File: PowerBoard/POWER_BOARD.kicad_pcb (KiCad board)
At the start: 4 copper layers, 152.1 x 80.1 mm, 158 parts, among them J1 B3B-XH-A_LF__SN_, J2 USB4145-03-0170-C_REVA2, J3 Molex Microfit 3.0, J5 Conn_02x10_Counter_Clockwise, J6 Molex Microfit 3.0, Q1 BSS138, Q2 FDD86250-F085, Q3 FGH50T65SQD-F155, Q4 BSS138, Q5 TN2130K1-G, Q6 STD11N60DM2, Q7 FGH50T65SQD-F155, T1 DA2034, U1 RPI2040, U10 PTS647SM38SMTR2LFS, U2 MCP14A0454-E/SN, U3 NCV1117DT33T5G, U4 LT3750, U5 W25Q16JVSNIQ, U6 LTC4151IMS_PBF, U7 MCP2515-xST, U8 MCP2551-I-SN, U9 PTS647SM38SMTR2LFS, Y1 ABM3-12.000MHZ-D2Y-T, Y2 ABM3-8.000MHZ-D2Y-T

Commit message: passed DRC check
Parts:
- Y2: footprint bots:445C25D12M00000 -> bots:ABM3
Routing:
- net Net-(C25-Pad2): track 6.77 -> 6.05 mm

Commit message: added pdfs
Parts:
- moved C2 52.2 mm to (119.7, 62.1)
- moved C3 52.2 mm to (119.7, 60.0)
- moved TP22 52.2 mm to (86.8, 64.6)
- moved R1 52.2 mm to (97.0, 58.0)
- moved R14 52.2 mm to (65.5, 42.5)
- moved R15 52.2 mm to (70.5, 42.5)
- moved R25 52.2 mm to (86.3, 45.9)
- moved TP17 52.2 mm to (109.8, 49.5)
- moved TP2 52.2 mm to (136.6, 41.4)
- moved TP9 52.2 mm to (117.4, 42.1)
- moved C13 52.2 mm to (74.3, 54.7)
- moved C15 52.2 mm to (83.0, 45.6)
- moved C19 52.2 mm to (75.0, 60.4)
- moved C20 52.2 mm to (90.1, 53.8)
- moved C23 52.2 mm to (90.1, 52.0)
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
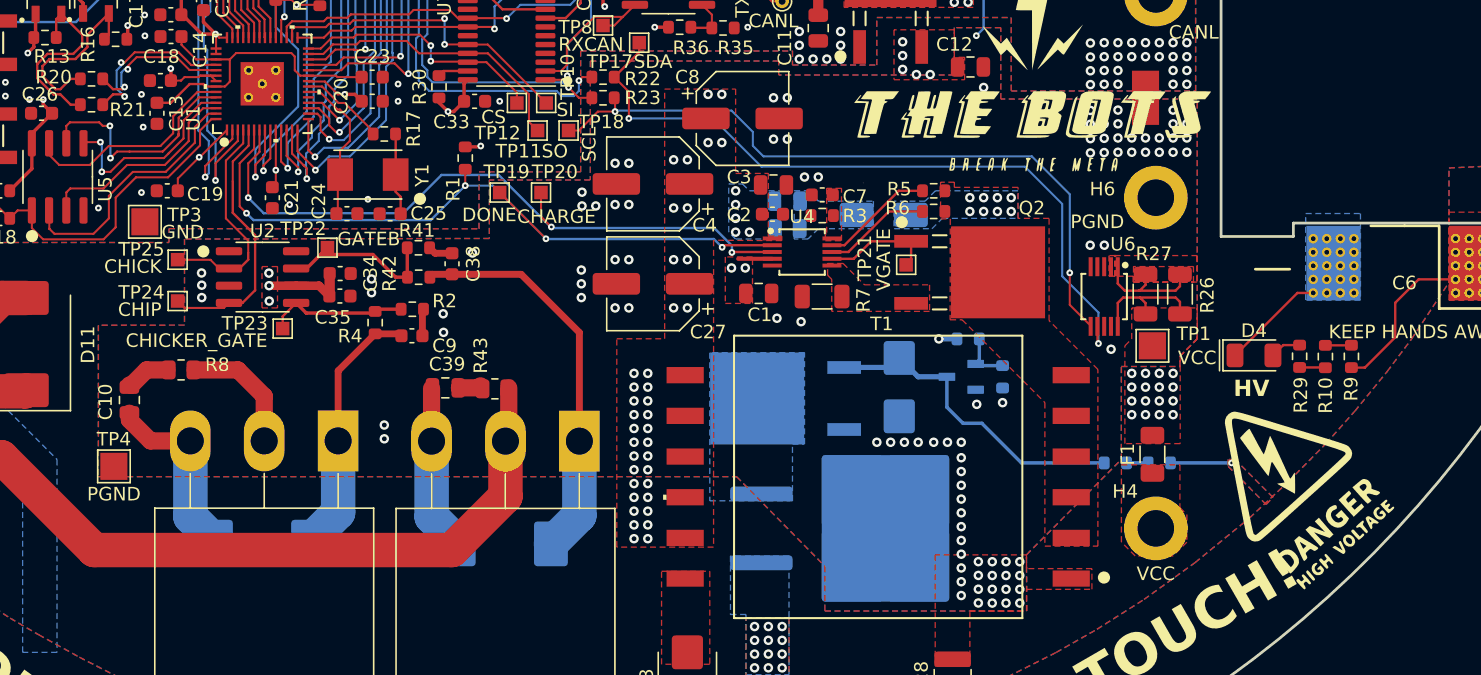
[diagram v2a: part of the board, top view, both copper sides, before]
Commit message: update to power board and midplate schematics
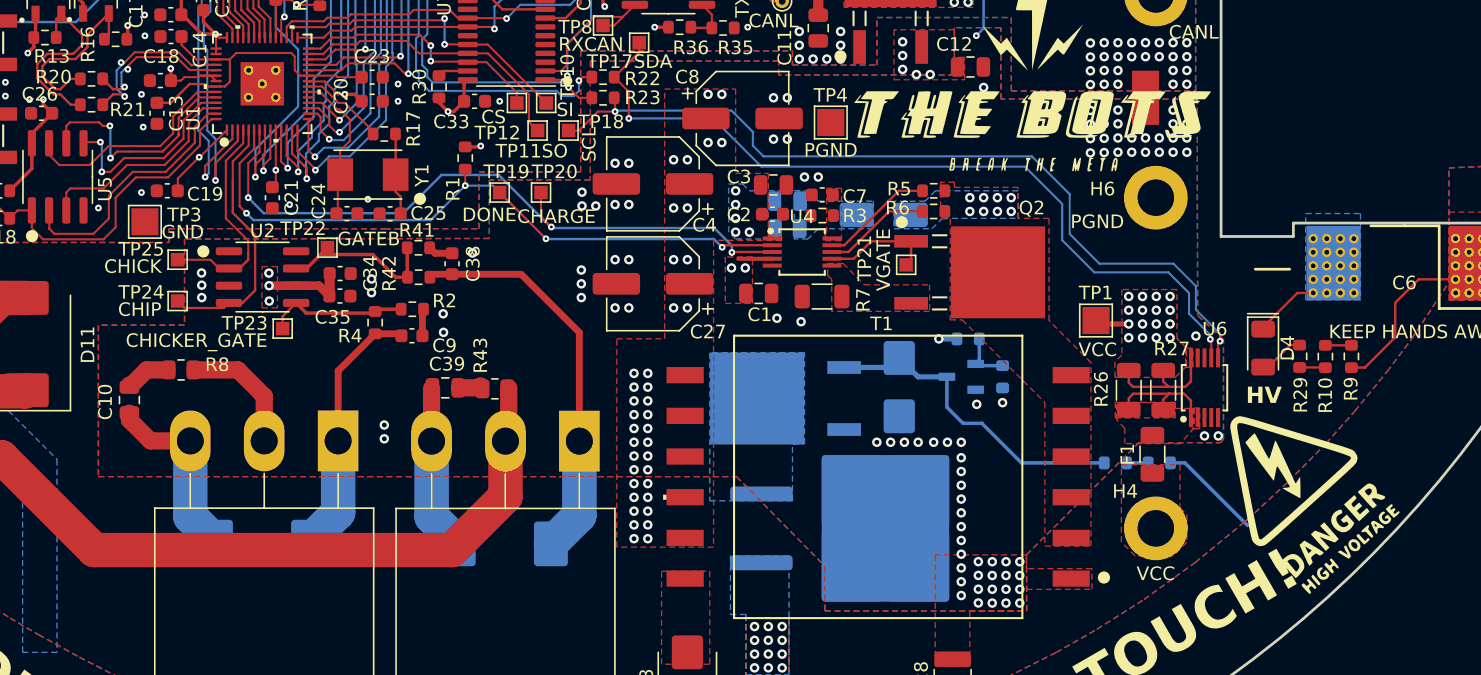
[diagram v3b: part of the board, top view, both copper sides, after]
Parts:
- moved TP4 58.6 mm to (124.0, 55.4)
- moved U6 10.00 mm to (151.5, 74.9), turned to 90 degrees
- moved R26 8.03 mm to (145.9, 75.1), turned to 90 degrees
- moved R27 7.21 mm to (148.5, 75.1), turned to 90 degrees
- moved TP1 4.56 mm to (143.5, 70.0)
- moved D4 0.86 mm to (155.8, 72.0), turned to -90 degrees
- moved G*** 0.52 mm to (158.1, 82.2)
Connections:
- F1 pad 2: VCC -> /Power/VCC_RPP
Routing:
- net /Power/U6SCL: track 52.1 -> 61.7 mm
- net /Power/U6SDA: track 54.1 -> 60.5 mm
- net HV: track 21.4 -> 24.5 mm, vias 13 -> 12
- net GNDPWR: track 37.7 -> 35.0 mm
- net VCC: track 31.1 -> 33.6 mm
- net Net-(D4-A): track 2.28 -> 3.37 mm

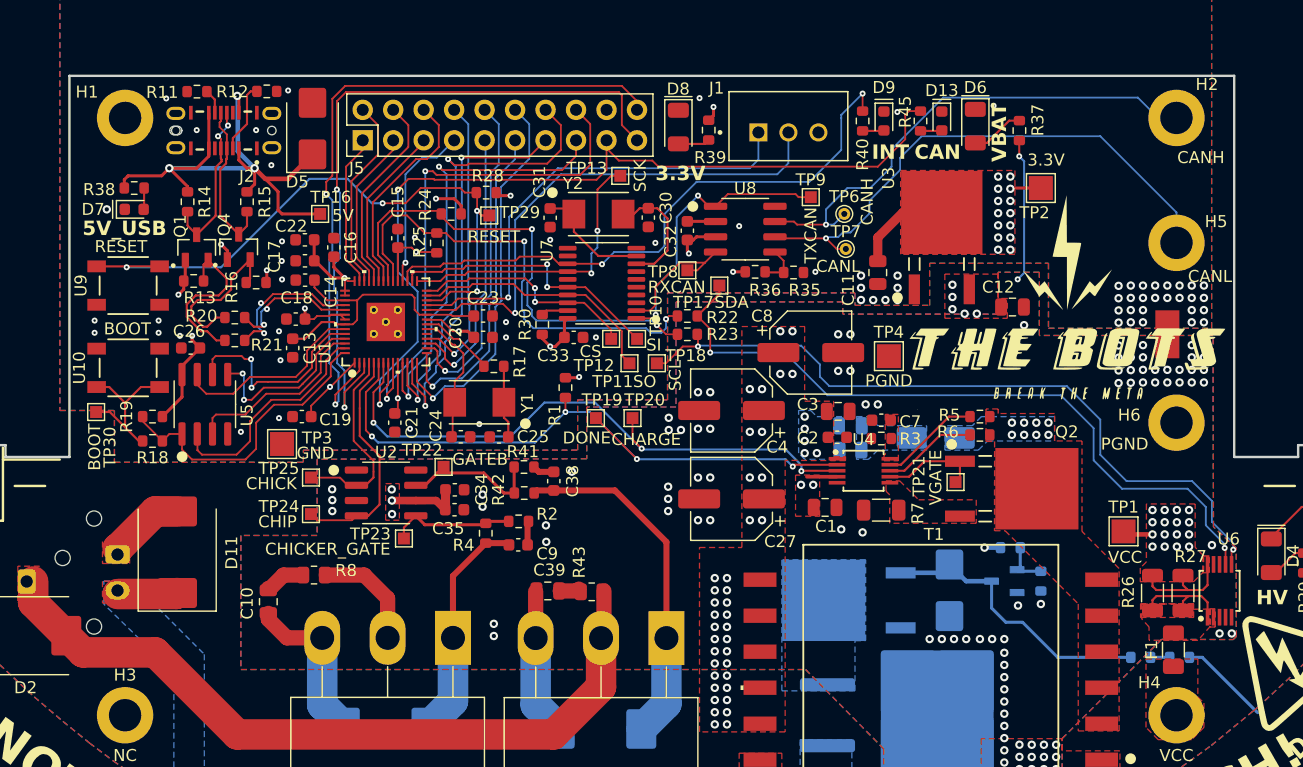
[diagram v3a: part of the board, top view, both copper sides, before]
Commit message: added switch and fuse
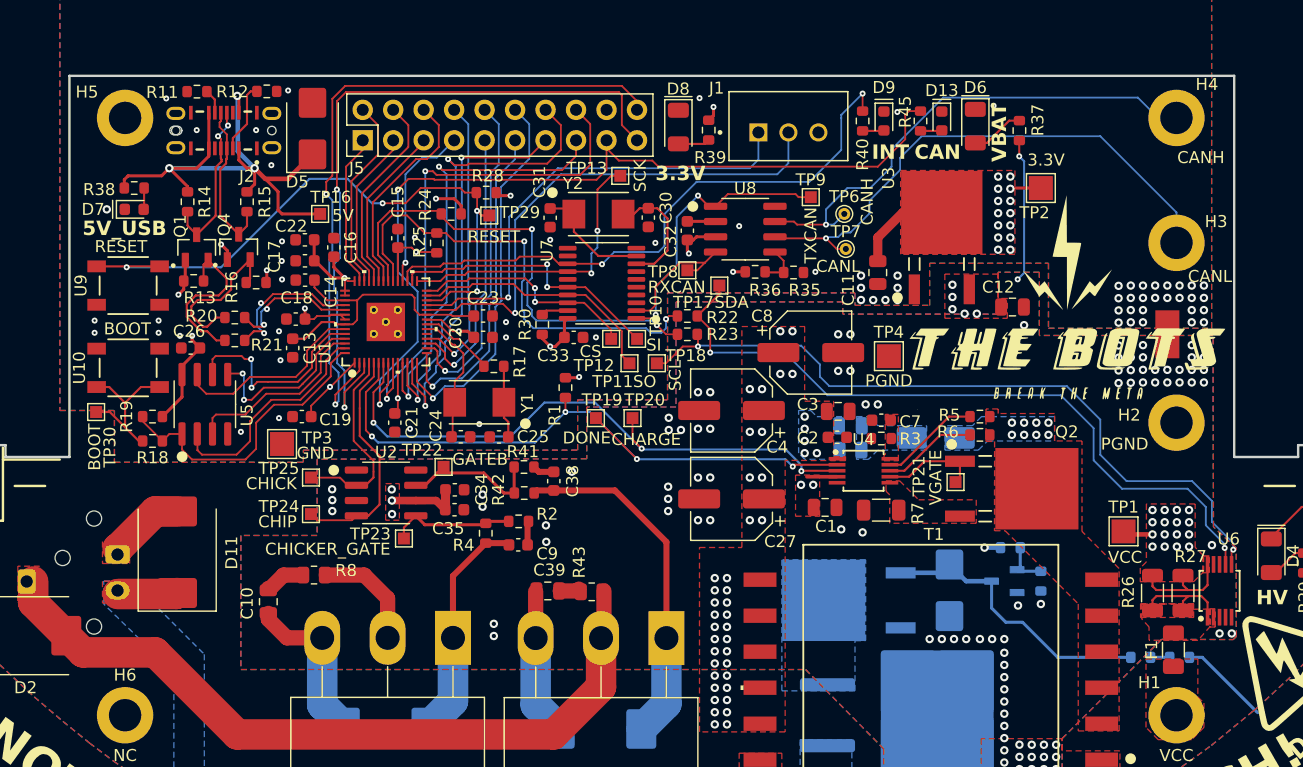
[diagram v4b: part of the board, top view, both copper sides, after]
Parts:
- renumbered H4 to H1, H6 to H2, H5 to H3, H2 to H4, H1 to H5, H3 to H6
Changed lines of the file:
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@@
   (net 108 "/Flyback_HV/AD_G")
   (net 109 "/Flyback_HV/AD_LV_G")
-  (net 110 "unconnected-(H1-Pad1)")
+  (net 110 "unconnected-(H5-Pad1)")
   (net 111 "/Power/VCC_FUSE")
   (net 112 "Net-(D13-A)")
-  (net 113 "unconnected-(H3-Pad1)")
+  (net 113 "unconnected-(H6-Pad1)")
   (net 114 "/Flyback_HV/RCD")
   (footprint "bots:C_0603_1608Metric" (layer "F.Cu")
@@
     (property "ki_keywords" "mounting hole")
     (attr exclude_from_pos_files)
-    (fp_text reference "H4" (at -2.2606 -2.7178) (layer "F.SilkS")
+    (fp_text reference "H1" (at -2.2606 -2.7178) (layer "F.SilkS")
         (effects (font (size 1 1) (thickness 0.15)))
     )
@@
     (property "ki_keywords" "mounting hole")
     (attr exclude_from_pos_files)
-    (fp_text reference "H3" (at 0 -3.35) (layer "F.SilkS")
+    (fp_text reference "H6" (at 0 -3.35) (layer "F.SilkS")
         (effects (font (size 1 1) (thickness 0.15)))
     )
@@
       (stroke (width 0.05) (type solid)) (fill none) (layer "F.CrtYd"))
     (pad "1" thru_hole circle (at 0 0) (size 4.7 4.7) (drill 2.7) (layers "*.Cu" "*.Mask")
-      (net 113 "unconnected-(H3-Pad1)") (pinfunction "1") (pintype "input+no_connect"))
+      (net 113 "unconnected-(H6-Pad1)") (pinfunction "1") (pintype "input+no_connect"))
   )
   (footprint "bots:TestPoint_Pad_1.0x1.0mm" (layer "F.Cu")
@@
     (property "ki_keywords" "mounting hole")
     (attr exclude_from_pos_files)
-    (fp_text reference "H5" (at 3.302 -1.778) (layer "F.SilkS")
+    (fp_text reference "H3" (at 3.302 -1.778) (layer "F.SilkS")
         (effects (font (size 1 1) (thickness 0.15)))
     )
@@
     (property "ki_keywords" "mounting hole")
     (attr exclude_from_pos_files)
-    (fp_text reference "H2" (at 2.54 -2.794) (layer "F.SilkS")
+    (fp_text reference "H4" (at 2.54 -2.794) (layer "F.SilkS")
         (effects (font (size 1 1) (thickness 0.15)))
     )
@@
     (property "ki_keywords" "mounting hole")
     (attr exclude_from_pos_files)
-    (fp_text reference "H6" (at -3.937 -0.635) (layer "F.SilkS")
+    (fp_text reference "H2" (at -3.937 -0.635) (layer "F.SilkS")
         (effects (font (size 1 1) (thickness 0.15)))
     )
@@
     (property "ki_keywords" "mounting hole")
     (attr exclude_from_pos_files)
-    (fp_text reference "H1" (at -3.175 -2.159) (layer "F.SilkS")
+    (fp_text reference "H5" (at -3.175 -2.159) (layer "F.SilkS")
         (effects (font (size 1 1) (thickness 0.15)))
     )
@@
       (stroke (width 0.05) (type solid)) (fill none) (layer "F.CrtYd"))
     (pad "1" thru_hole circle (at 0 0) (size 4.7 4.7) (drill 2.7) (layers "*.Cu" "*.Mask")
-      (net 110 "unconnected-(H1-Pad1)") (pinfunction "1") (pintype "input+no_connect"))
+      (net 110 "unconnected-(H5-Pad1)") (pinfunction "1") (pintype "input+no_connect"))
   )
   (footprint "bots:C_0603_1608Metric" (layer "F.Cu")

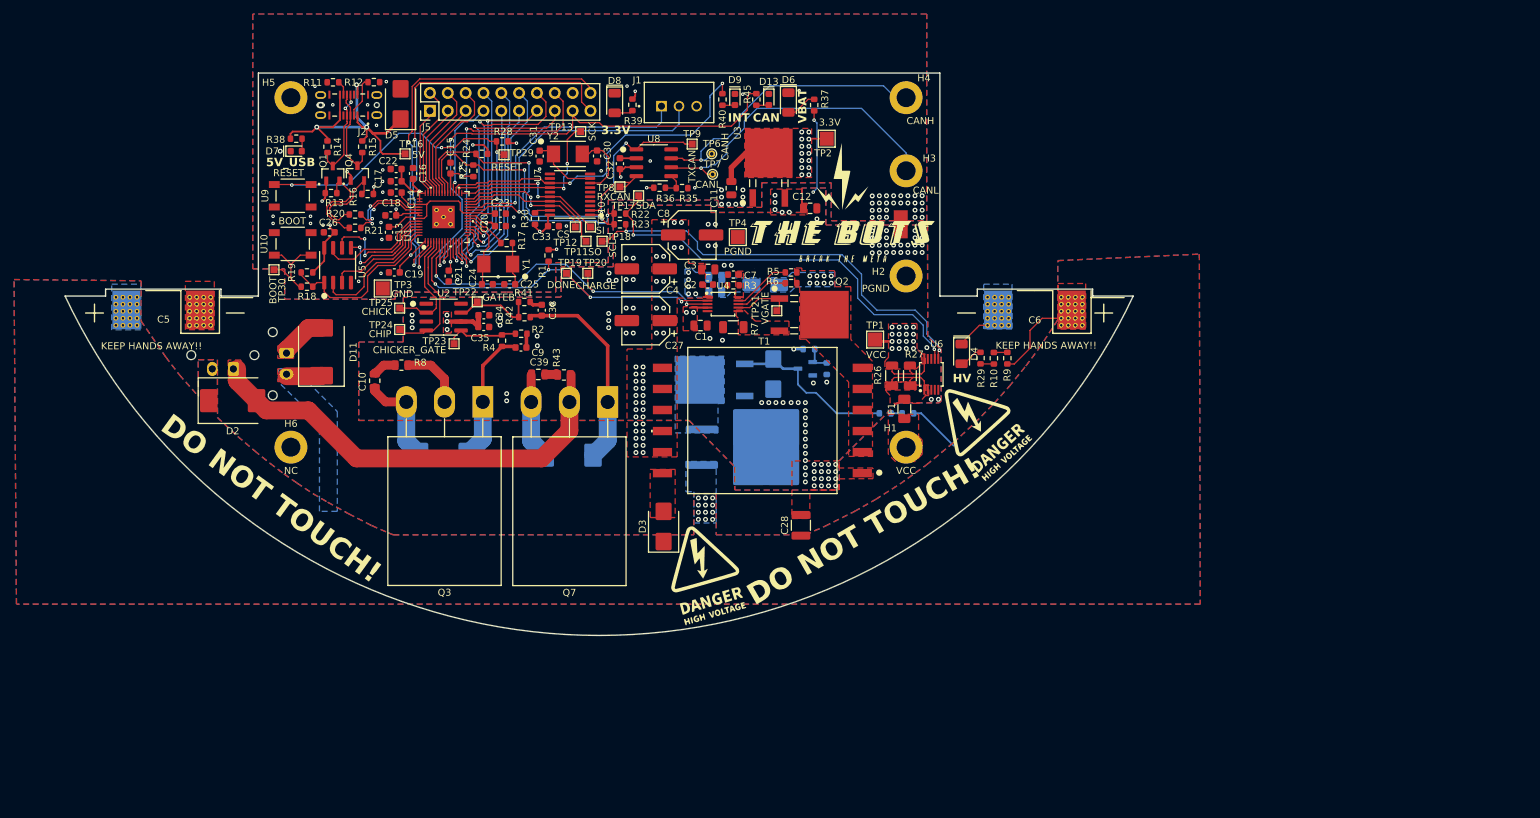
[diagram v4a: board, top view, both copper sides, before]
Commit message: powerboard HV powerpillars + midplate
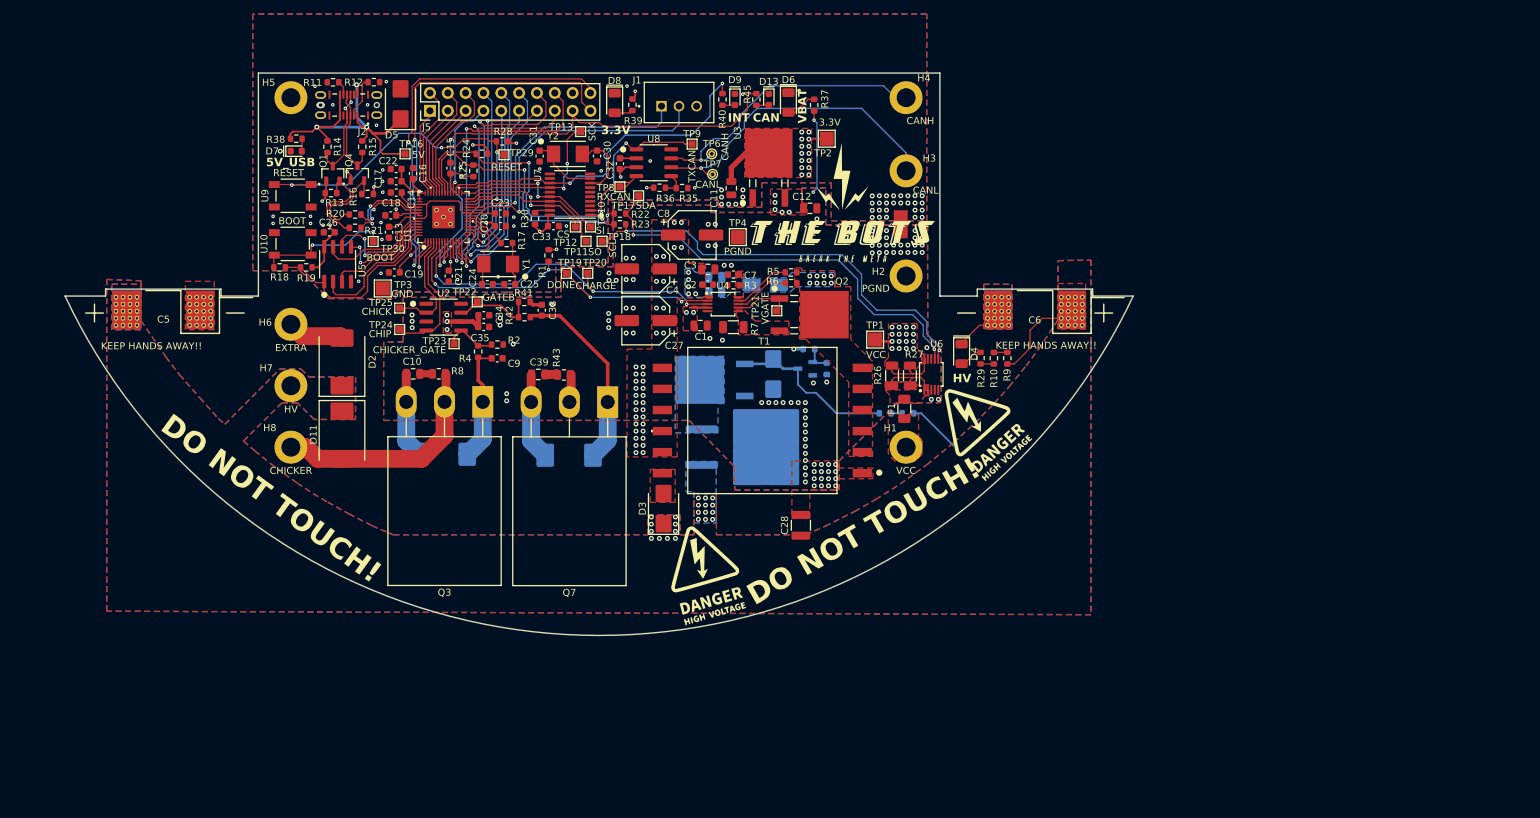
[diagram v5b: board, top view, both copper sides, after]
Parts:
- removed J3, J6: Molex Microfit 3.0, bots:Molex_Micro-Fit_3.0_43650-0215_1x02_P3.00mm_Vertical
- added H6: EXTRA, bots:MountingHole_2.7mm_M2.5_DIN965_Pad, F.Cu at (60.3, 67.8)
- added H7: HV, bots:MountingHole_2.7mm_M2.5_DIN965_Pad, F.Cu at (60.3, 76.6)
- H8: renamed from H6; value NC -> CHICKER
- moved D2 16.5 mm to (67.6, 73.2), turned to 90 degrees
- moved TP30 14.7 mm to (72.0, 56.0)
- moved D11 12.2 mm to (67.6, 83.6), turned to -90 degrees
- moved C10 5.56 mm to (77.7, 74.9), turned to 180 degrees
- moved R8 5.46 mm to (81.4, 74.8)
- moved R18 4.78 mm to (58.7, 59.7)
- moved C9 3.72 mm to (89.7, 72.6)
- moved R4 3.72 mm to (87.0, 71.7)
- moved R2 3.72 mm to (89.7, 70.7)
- moved D3 2.54 mm to (113.4, 94.1)
- moved R19 0.73 mm to (62.5, 59.7)
- moved U5 0.14 mm to (66.9, 59.2)
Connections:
- net /Flyback_HV/EXTRA_HV renamed EXTRA_HV
- net Net-(C10-Pad1) renamed /Flyback_HV/SNUB2
- D11 pad 2: /Flyback_HV/CHICKER_HV -> CHICKER_HV
- H8 pad 1: unconnected-(H6-Pad1) -> CHICKER_HV
- Q3 pad 2: /Flyback_HV/CHICKER_HV -> CHICKER_HV
- R8 pad 1: /Flyback_HV/CHICKER_HV -> CHICKER_HV
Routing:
- net /Flyback_HV/CHICKER_HV: track 43.3 -> 0.00 mm
- net CHICKER_HV: track 0.00 -> 32.9 mm
- net /RP2040_CAN_FLASH/BOOT: track 13.2 -> 19.4 mm, vias 0 -> 2
- net HV: track 24.5 -> 19.5 mm, vias 12 -> 22
- net EXTRA_HV: track 63.4 -> 59.7 mm
- net GNDPWR: track 35.0 -> 31.3 mm, vias 98 -> 97
- net /Flyback_HV/CHICKER_GATE: track 10.5 -> 7.63 mm
- net /Flyback_HV/IGBTGATE_CHICKER: track 19.4 -> 17.0 mm
- net /RP2040_CAN_FLASH/QSPI_SS: track 25.4 -> 27.3 mm
- net /Flyback_HV/IGBTGATE_EXTRA: track 29.3 -> 27.9 mm
- net /Flyback_HV/SNUB2: track 3.24 -> 1.79 mm
- removed copper zone on F.Cu, net /Flyback_HV/CHICKER_HV
- removed copper zone on In1.Cu, net /Flyback_HV/CHICKER_HV
- removed copper zone on F.Cu, net EXTRA_HV
